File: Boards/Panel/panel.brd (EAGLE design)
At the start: 81.3 x 99.1 mm, 48 parts, among them IC301 MAX232SOIC16, J101 PN61729-S, J401 POWER_IN, J402 OPTRONIK, J403 BUTTON, J404 VIA/JETSON, J405 JOYSTICK, J406 MONITOR, J407 RESV, J408 INDICATOR, T101 MMBT2222A, U201 PSU_5V, U202 PSU_12V, U301 CAN_INTERFACE

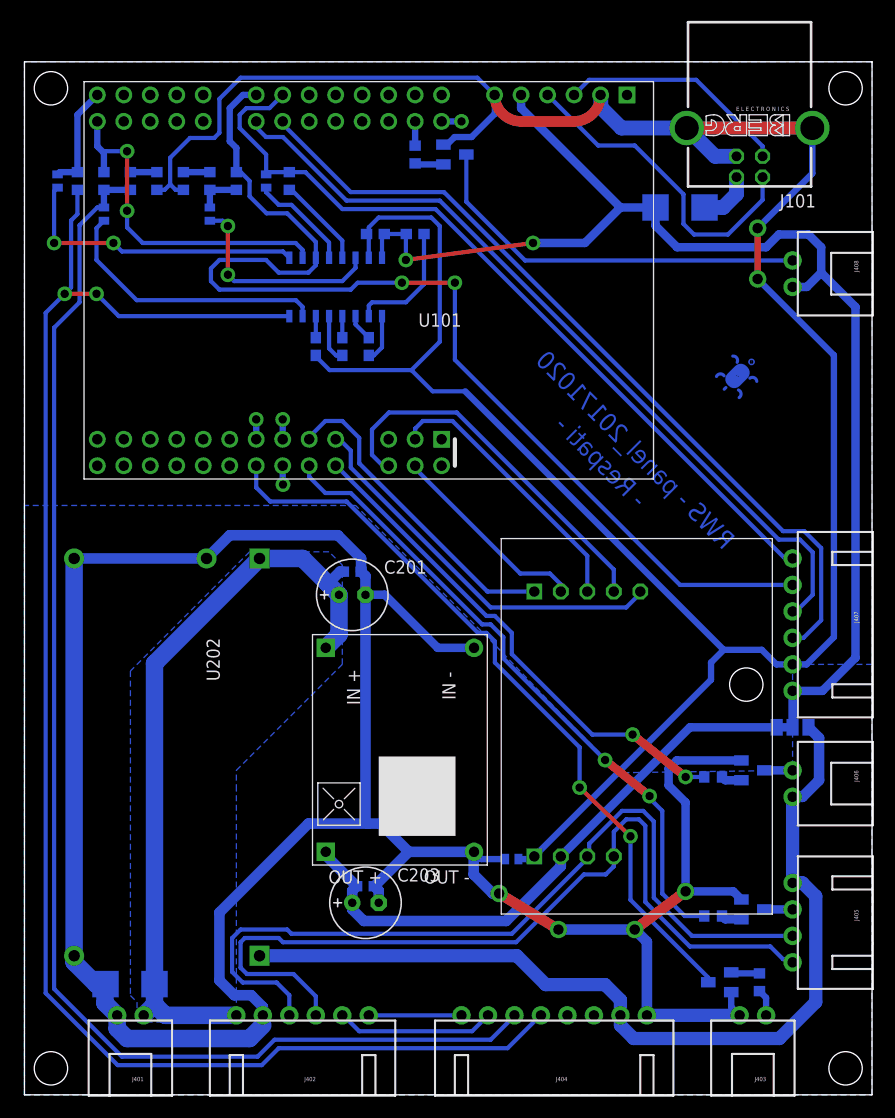
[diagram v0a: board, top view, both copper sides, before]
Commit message: add extBoard & update panel & motorControl board
> update panel board
> update motorControl board
>add extBoard:
  - to replace mouse movement & left/right click
  - add clear target button
  - add manual lrf value manually using keypad and display it on 4 digits 7-segment
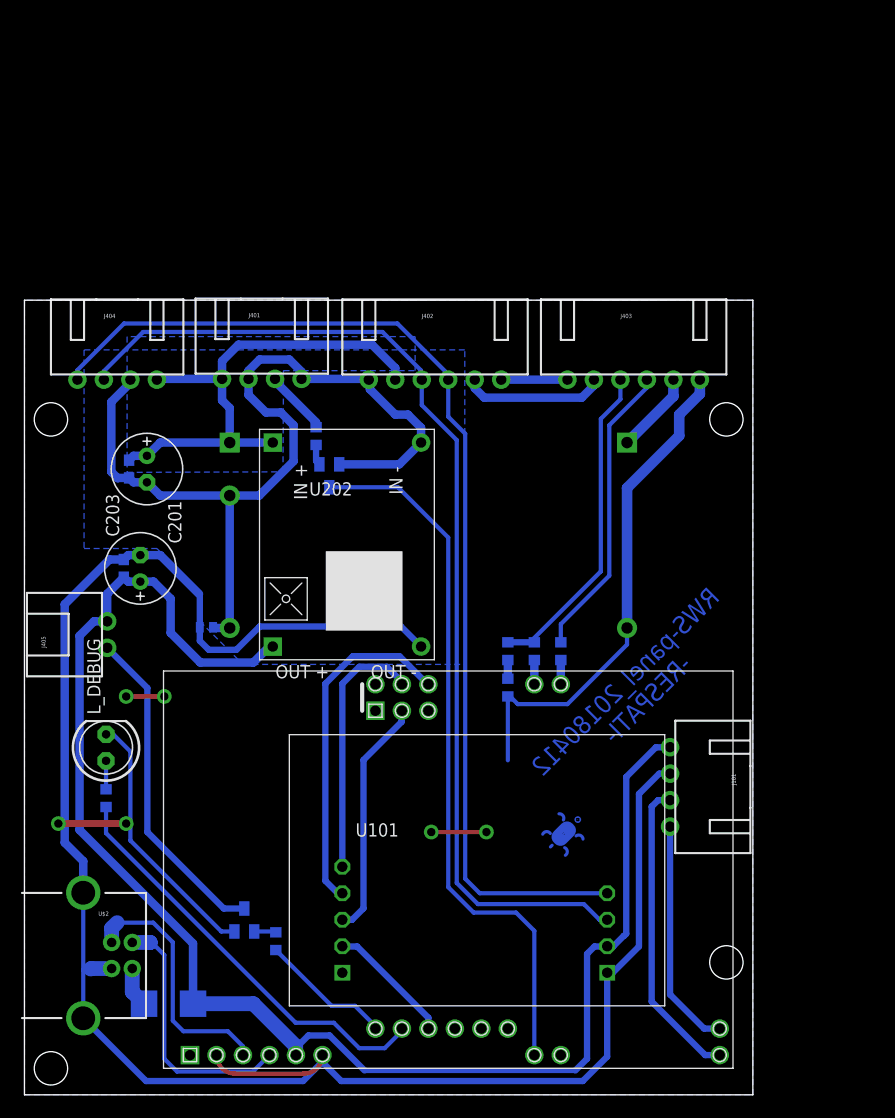
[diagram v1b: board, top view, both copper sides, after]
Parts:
- removed C301, C302, C303, C304, C305: 100n, resistor:C0603
- removed D401: 1N5822, adafruit:SMADIODE
- removed IC301: MAX232SOIC16, SparkFun-DigitalIC:SO016
- removed J406: MONITOR, SparkFun-Connectors:XH-2-RA
- removed J407: RESV, SparkFun-Connectors:XH-6-RA
- removed J408: INDICATOR, SparkFun-Connectors:XH-2-RA
- removed R301: 100, rcl:R0603
- removed R302, R306: 100R, rcl:R0603
- removed R303, R304, R305: 1k, rcl:R0603
- removed R307, R308, R309: 10k, rcl:R0603
- removed R401, R402, R403: 1k, resistor:R0603
- removed SJ301, SJ302, SJ303, SJ304: (no value), jumper:SJS
- removed SJ401: (no value), jumper:SJ_2
- removed T401, T402: (no value), transistor:SOT23-BEC
- removed U301: CAN_INTERFACE, scorpion:MCP2515_CAN
- added L_DEBUG: (no value), adafruit:LED5MM
- added R101, R4: 100, rcl:R0603
- added R102, R103: 1k, resistor:R0603
- added R5, R6, R7: 1k, rcl:R0603
- added U$2: USB+SHIELD, SparkFun:USB-B-PTH
- added U$3: MOD_MEGA_LAYOUT_SERIAL1, encPhone:MOD_MEGA_LAYOUT_SERIAL1
- added U$4: MOD_MEGA_LAYOUT_SERIAL2, encPhone:MOD_MEGA_LAYOUT_SERIAL2
- added U$5: MOD_MEGA_LAYOUT_SERIAL3, encPhone:MOD_MEGA_LAYOUT_SERIAL3
- added U$6: MOD_MEGA_LAYOUT_ICSP, encPhone:MOD_MEGA_LAYOUT_ICSP
- added U$7: MOD_MEGA_LAYOUT_Y_EVEN, encPhone:MOD_MEGA_LAYOUT_Y_EVEN
- added U1: (no value), scorpion:MCP2515_CAN2
- J101: value PN61729-S -> RESV; device con-berg:PN61729-S -> SparkFun-Connectors:XH-4-RA
- J401: device SparkFun-Connectors:XH-2-RA -> SparkFun-Connectors:XH-4-RA
- J403: value BUTTON -> JETSON; device SparkFun-Connectors:XH-2-RA -> SparkFun-Connectors:XH-6-RA
- J404: value VIA/JETSON -> JOYSTICK+MONITOR; device SparkFun-Connectors:XH-8-RA -> SparkFun-Connectors:XH-4-RA
- J405: value JOYSTICK -> INDICATOR; device SparkFun-Connectors:XH-4-RA -> SparkFun-Connectors:XH-2-RA
- U101: value (none) -> MODULE_MEGA2560; device encPhone:MODULE_MEGA -> encPhone:MOD_MEGA_LAYOUT
- moved U101 105.6 mm to (13.3, 2.54), turned to 0 degrees
- moved D101 90.7 mm to (13.8, 8.74), turned to 0 degrees
- moved T403 76.1 mm to (21.1, 16.8), turned to 0 degrees
- moved J404 74.0 mm to (8.89, 68.6), turned to 0 degrees
- moved J405 71.3 mm to (7.94, 44.1), turned to 90 degrees
- moved U202 68.9 mm to (62.2, 41.6), turned to 0 degrees
- moved J101 63.6 mm to (61.9, 29.5), turned to 270 degrees
- moved J401 62.3 mm to (22.8, 68.7), turned to 0 degrees
- moved J402 62.3 mm to (39.4, 68.6), turned to 0 degrees
- moved J403 62.0 mm to (58.4, 68.6), turned to 0 degrees
- moved T101 61.3 mm to (29.2, 59.4), turned to 180 degrees
- moved U$1 46.9 mm to (51.7, 25.0)
- moved C203 38.7 mm to (11.1, 50.5), turned to 90 degrees
- moved C204 38.3 mm to (9.53, 50.5), turned to 90 degrees
- moved SJ201 36.8 mm to (17.4, 44.8), turned to 0 degrees
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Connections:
- removed net +12V: J404.2, J405.1, J406.2, SJ401.3, U202.2
- removed net BUS_INT: U101.X3, U301.5
- removed net INDICATOR: R403.2, U101.Y4
- removed net JS_PWR_ENABLE: R402.2, U101.X4
- removed net MONITOR_PWR_ENABLE: R401.2, U101.X2
- removed net N$10: IC301.14, SJ304.1
- removed net N$2: IC301.9, SJ301.2
- removed net N$3: IC301.7, SJ302.1
- removed net N$84: C302.1, IC301.3
- removed net N$85: C303.1, IC301.5
- removed net N$86: C302.2, IC301.1
- removed net N$87: C303.2, IC301.4
- removed net N$88: C304.1, IC301.2
- removed net N$89: C305.1, IC301.6
- removed net N$9: J406.1, T401.C
- removed net N$95: R304.1, R305.2
- removed net N$96: R301.2, T101.1
- removed net RESV1: U101.X6
- removed net RESV2: U101.X7
- removed net RESV3: U101.Y2
- removed net RESV_RX: R307.2, R308.2, SJ304.2
- removed net RESV_TX: IC301.13, R306.1
- removed net SCL: J407.4, U101.Y14
- removed net SDA: J407.3, U101.Y13
- removed net USB_D+: J101.3, U101.P3
- removed net USB_D-: J101.2, U101.P4
- removed net VIA_RX: J404.6, R303.2, R304.2, SJ302.2
- removed net VIA_RXD: IC301.10, R303.1, U101.Z10
- removed net VIA_TX: IC301.8, J404.5, R302.1
- removed net VIA_TXD: R302.2, SJ301.1, U101.Z9
- new net +15V: J403.5, U202.2
- new net INDICATOR_RTN: J405.1, T403.C
- new net JETSON_RX: J403.3, R5.1, R6.1
- new net JETSON_RXD: R5.2, U$4.X5
- new net JETSON_TX: J403.4, R4.1
- new net JETSON_TXD: R4.2, U$4.X8
- new net N$14: R6.2, R7.1
- net +24V: now also J402.2, J404.4; no longer D401.C, J402.6
- net BUS_CANH: now also J402.3, J404.2, U1.3; no longer J402.4, J405.3, U301.3
- net BUS_CANL: now also J402.4, J404.1, U1.4; no longer J402.3, J405.4, U301.4
- net BUS_CS: now also U$7.Y6, U1.6; no longer U101.X1, U301.9
- net BUTTON_RXD: now also U$3.Y15; no longer U101.X5
- net BUTTON_TX: now also J401.3, R101.1; no longer J403.1, R301.1
- net BUTTON_TXD: now also U$3.Y16; no longer U101.X8
- net GND: now also C203.-, C204.2, J101.2, J403.6, L_DEBUG.K, R7.2, U$2.GND, U$2.S1, U$2.S2, U1.1, U201.4, U202.4; no longer C301.2, C305.2, IC301.15, J101.4, J101.S1, J101.S2, J407.5, R305.1, R309.1, U301.1
- net MISO: now also U$6.S6, U1.8; no longer U101.S6, U301.8
- net MOSI: now also U$6.S3, U1.7; no longer U101.S3, U301.7
- net N$1: now also R102.1; no longer R403.1
- net N$11: now also L_DEBUG.A, R103.1; no longer R308.1, R309.2
- net N$12: now also R103.2, U$7.Y4; no longer D101.A, J101.1
- net N$4: now also U$2.D+, U101.P3; no longer R401.1, T401.B
- net N$5: now also U$2.D-, U101.P4; no longer J405.2, T402.C
- net N$6: now also D101.A, U$2.VBUS; no longer R402.1, T402.B
- net N$7: now also R102.2, U$7.Y2; no longer J408.1, T403.C
- net N$8: now also R101.2, T101.1; no longer IC301.12, SJ303.2
- net RESV_RXD: now also J101.4, U$5.Z10; no longer IC301.11, J407.2, R307.1, U101.Y15
- net RESV_TXD: now also J101.3, U$5.Z9; no longer J407.1, R306.2, SJ303.1, U101.Y16
- net SCK: now also U$6.S4, U1.9; no longer U101.S4, U301.6
- net V-: now also J401.4, J402.1, J404.3; no longer C203.-, C204.2, D401.A, J402.5, J403.2, J404.1, T401.E, T402.E, U201.4, U202.4
- net VCC: now also J101.1, J405.2, U1.2; no longer C301.1, C304.2, IC301.16, J407.6, J408.2, SJ401.1, SJ401.2, U301.2
- net VIDEO+: now also J402.5, J403.2; no longer J402.2, J404.7
- net VIDEO-: now also J402.6, J403.1; no longer J402.1, J404.8
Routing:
- net V-: track 252.2 -> 85.7 mm, vias 4 -> 0
- net VIA_TX: track 153.1 -> 0.00 mm, vias 2 -> 0
- net VIA_RX: track 130.0 -> 0.00 mm
- net +12V: track 89.4 -> 0.00 mm
- net RESV_RXD: track 108.1 -> 22.2 mm, vias 2 -> 0
- net SCL: track 79.1 -> 0.00 mm
- net SDA: track 77.5 -> 0.00 mm
- net JS_PWR_ENABLE: track 62.1 -> 0.00 mm, vias 2 -> 0
- net MONITOR_PWR_ENABLE: track 48.6 -> 0.00 mm, vias 2 -> 0
- net RESV_TXD: track 77.6 -> 29.4 mm
- net N$12: track 5.22 -> 40.3 mm
- net VCC: track 179.4 -> 145.8 mm, vias 2 -> 0
- net VIA_RXD: track 33.2 -> 0.00 mm, vias 2 -> 0
- net INDICATOR_RTN: track 0.00 -> 31.6 mm
- net USB_D-: track 31.4 -> 0.00 mm
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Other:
- board size 81.3 x 99.1 mm -> 69.8 x 76.2 mm
- board text added: "-RESPATI-"
- board text added: "RWS-panel_20180412"
- board text removed: "- Respati -"
- board text removed: "RWS - panel_20171020"
